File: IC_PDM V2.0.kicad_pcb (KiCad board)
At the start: 2 copper layers, 118 x 78 mm, 15 parts, among them J10 Conn_01x04, J11 Conn_01x04, J12 Conn_01x04, J13 Conn_01x04, J14 Conn_01x04, J15 Conn_01x04, J16 Conn_01x02, J3 S03B-XASK-1, J4 S03B-XASK-1, J5 Conn_01x02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

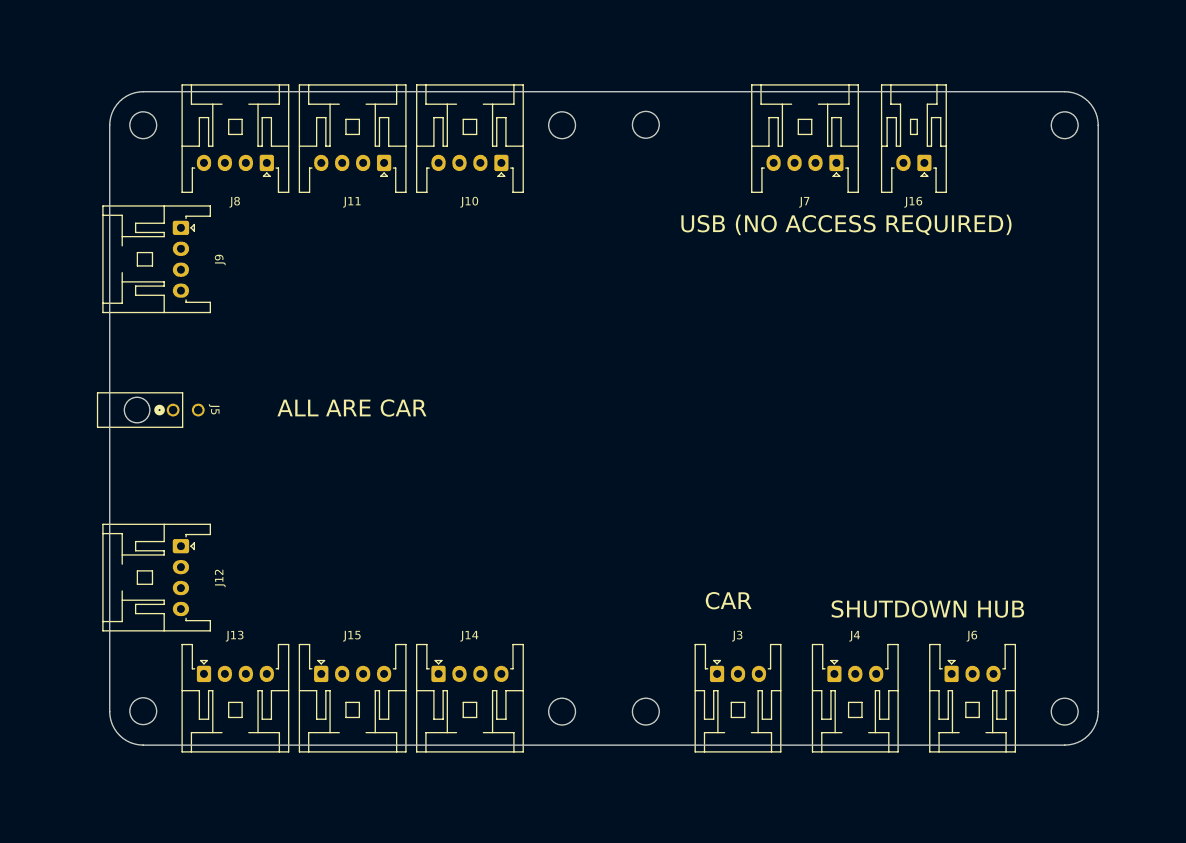
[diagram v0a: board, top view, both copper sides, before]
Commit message: Bosh
Routed PCB and fixed schematic
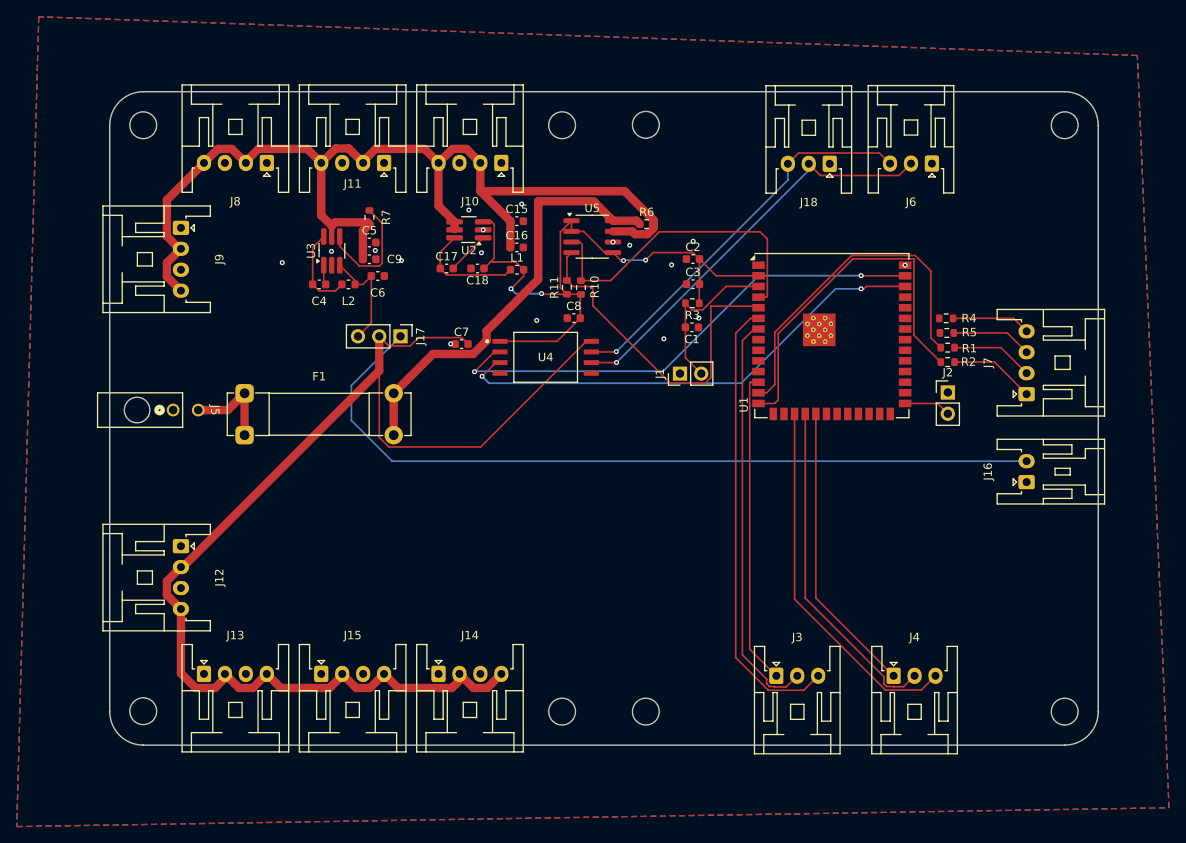
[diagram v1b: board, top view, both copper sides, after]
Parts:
- added C1: 1u, Capacitor_SMD:C_0603_1608Metric, F.Cu at (126.5, 80.1)
- added C15: 2.2u, Capacitor_SMD:C_0603_1608Metric, F.Cu at (105.6, 67.5)
- added C16: 100n, Capacitor_SMD:C_0603_1608Metric, F.Cu at (105.6, 70.6)
- added C17: 100n, Capacitor_SMD:C_0603_1608Metric, F.Cu at (97.2, 73.1)
- added C18: 10u, Capacitor_SMD:C_0603_1608Metric, F.Cu at (100.9, 73.1)
- added C2: 22u, Capacitor_SMD:C_0603_1608Metric, F.Cu at (126.6, 72.0)
- added C3: 0.1u, Capacitor_SMD:C_0603_1608Metric, F.Cu at (126.6, 75.0)
- added C4: 100n, Capacitor_SMD:C_0603_1608Metric, F.Cu at (82.0, 75.0)
- added C5: 10u, Capacitor_SMD:C_0603_1608Metric, F.Cu at (88.0, 70.0)
- added C6: 22u, Capacitor_SMD:C_0603_1608Metric, F.Cu at (89.0, 74.0)
- added C7: 0.1u, Capacitor_SMD:C_0603_1608Metric, F.Cu at (99.0, 82.1)
- added C8: 0.1u, Capacitor_SMD:C_0603_1608Metric, F.Cu at (112.4, 79.0)
- added C9: 100n, Capacitor_SMD:C_0603_1608Metric, F.Cu at (88.0, 72.0)
- added F1: Fuse, Fuse:Fuseholder_Clip-5x20mm_Bel_FC-203-22_Lateral_P17.80x5.00mm_D1.17mm_Horizontal, F.Cu at (73.1, 88.0)
- added J1: RST, Connector_PinHeader_2.54mm:PinHeader_1x02_P2.54mm_Vertical, F.Cu at (125.1, 85.7)
- added J17: Conn_01x03, Connector_PinHeader_2.54mm:PinHeader_1x03_P2.54mm_Vertical, F.Cu at (91.7, 81.2)
- added J18: S03B-XASK-1, Connector_JST:JST_XA_S03B-XASK-1_1x03_P2.50mm_Horizontal, F.Cu at (142.9, 60.6)
- added J2: BSEL, Connector_PinHeader_2.54mm:PinHeader_1x02_P2.54mm_Vertical, F.Cu at (157.1, 87.9)
- added L1: 3.9u, Inductor_SMD:L_0603_1608Metric, F.Cu at (105.6, 73.2)
- added L2: 5.6u, Inductor_SMD:L_0603_1608Metric, F.Cu at (85.5, 75.0)
- added R1: 27, Resistor_SMD:R_0603_1608Metric, F.Cu at (157.0, 82.5)
- added R10: 4k7, Resistor_SMD:R_0603_1608Metric, F.Cu at (113.2, 75.4)
- added R11: 4k7, Resistor_SMD:R_0603_1608Metric, F.Cu at (111.6, 75.3)
- added R2: 27, Resistor_SMD:R_0603_1608Metric, F.Cu at (157.0, 84.3)
- added R3: 10k, Resistor_SMD:R_0603_1608Metric, F.Cu at (126.5, 77.2)
- added R4: 5k1, Resistor_SMD:R_0603_1608Metric, F.Cu at (156.8, 79.0)
- added R5: 5k, Resistor_SMD:R_0603_1608Metric, F.Cu at (156.9, 80.8)
- added R6: 0.1, Resistor_SMD:R_0603_1608Metric, F.Cu at (121.1, 67.8)
- added R7: 0, Resistor_SMD:R_0603_1608Metric, F.Cu at (88.0, 67.0)
- added U1: ESP32-S3-WROOM-1U-N4R2, RF_Module:ESP32-S3-WROOM-1U, F.Cu at (143.2, 81.1)
- added U2: LMR50410Y3FQDBVRQ1, Custom_MSM:Regulator_Switching_SOT-23-6, F.Cu at (99.9, 68.5)
- added U3: LMR50410Y5FQDBVRQ1, Custom_MSM:Regulator_Switching_SOT-23-6, F.Cu at (83.5, 71.0)
- added U4: ISO1042BQDWVQ1, customFootprints:DWV0008A-MFG, F.Cu at (109.0, 83.7)
- added U5: INA219AxD, Package_SO:SOIC-8_3.9x4.9mm_P1.27mm, F.Cu at (114.6, 69.3)
- moved J6 61.0 mm to (155.2, 60.6), turned to 180 degrees
- moved J16 40.0 mm to (166.4, 98.6), turned to 90 degrees
- moved J7 35.7 mm to (166.4, 88.1), turned to 90 degrees
- moved J3 7.08 mm to (136.6, 121.7)
- moved J4 7.08 mm to (150.6, 121.7)
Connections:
- J16 pad 1: unconnected-(J16-Pin_1-Pad1) -> GND
- J16 pad 2: unconnected-(J16-Pin_2-Pad2) -> +5V_USB
- J7 pad 1: unconnected-(J7-Pin_1-Pad1) -> USBD+
- J7 pad 2: unconnected-(J7-Pin_2-Pad2) -> USBD-
- J7 pad 3: unconnected-(J7-Pin_3-Pad3) -> Net-(J7-Pin_3)
- J7 pad 4: unconnected-(J7-Pin_4-Pad4) -> Net-(J7-Pin_4)
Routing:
- net +5V: track 0.00 -> 153.9 mm
- net +12V: track 0.00 -> 125.4 mm
- net +5V_USB: track 0.00 -> 95.1 mm
- net +3V3: track 0.00 -> 78.6 mm, vias 0 -> 4
- net CAND: track 0.00 -> 60.2 mm, vias 0 -> 2
- net CANR: track 0.00 -> 58.4 mm, vias 0 -> 2
- net BSPD: track 0.00 -> 54.4 mm
- net LVMS: track 0.00 -> 51.1 mm
- net CANL: track 0.00 -> 49.6 mm, vias 0 -> 1
- net CKPT: track 0.00 -> 49.0 mm
- net CANH: track 0.00 -> 47.2 mm, vias 0 -> 1
- net RIGHT: track 0.00 -> 44.1 mm
- net Net-(U1-IO20): track 0.00 -> 44.0 mm
- net SCL: track 0.00 -> 41.7 mm
- net Net-(U1-IO19): track 0.00 -> 41.4 mm
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- added copper zone on B.Cu, net GND
- added copper zone on F.Cu, net GND
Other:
- board text removed: "ALL ARE CAR"
- board text removed: "CAR"
- board text removed: "SHUTDOWN HUB"
- board text removed: "USB (NO ACCESS REQUIRED)"
